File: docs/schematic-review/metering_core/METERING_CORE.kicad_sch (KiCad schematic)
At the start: 56 parts, among them U2 ATM90E26-YU, U4 ISO6721BD, U5 MAX3487E

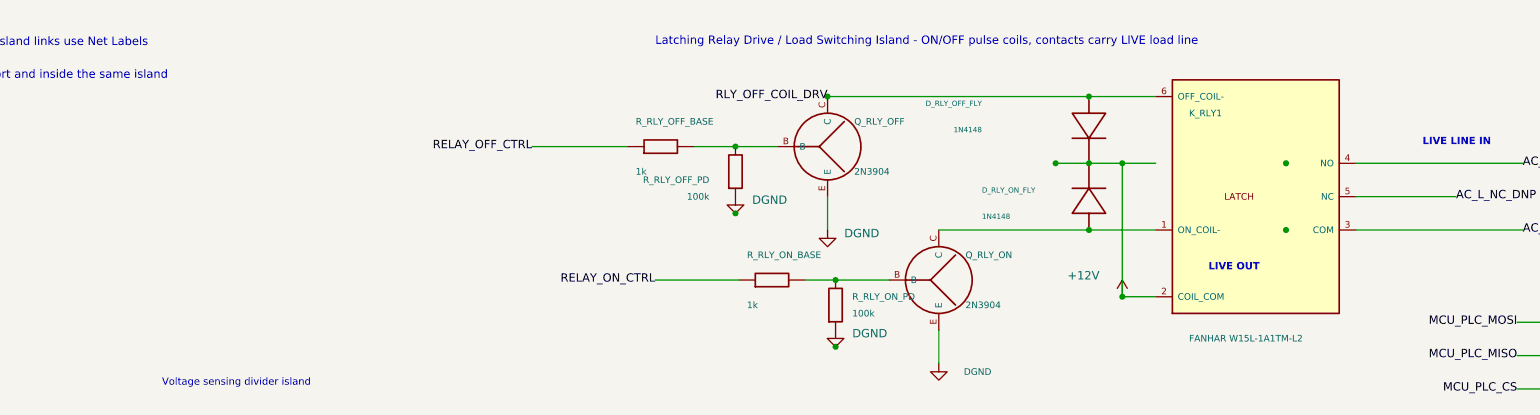
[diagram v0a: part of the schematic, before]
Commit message: Fix latching relay coil common routing
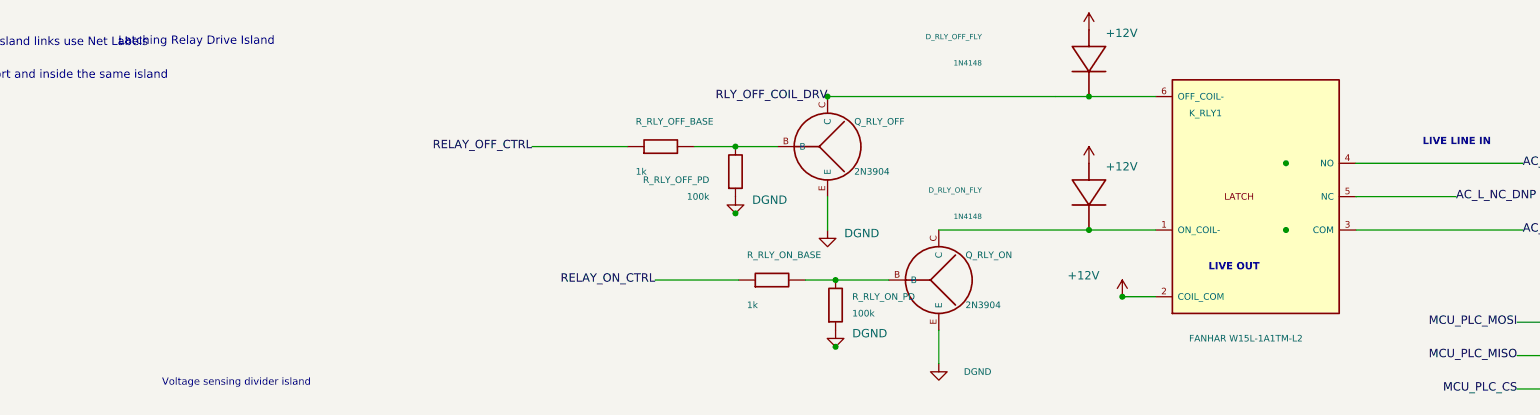
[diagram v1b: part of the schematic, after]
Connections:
- net +12V: now also D_RLY_OFF_FLY.A, D_RLY_ON_FLY.A; no longer D_RLY_OFF_FLY.K, D_RLY_ON_FLY.K
- net RLY_OFF_COIL_DRV: now also D_RLY_OFF_FLY.K; no longer D_RLY_OFF_FLY.A
- net at K_RLY1.1 (ON_COIL-), Q_RLY_ON.C: now also D_RLY_ON_FLY.K; no longer D_RLY_ON_FLY.A
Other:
- note added: "Latching Relay Drive Island"
- note removed: "Latching Relay Drive / Load Switching Island - ON/OFF pulse coils, contacts carry LIVE load line"
- moved on the sheet: D_RLY_OFF_FLY, D_RLY_ON_FLY
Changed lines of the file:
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@@
 		)
 	)
-	(text "Latching Relay Drive / Load Switching Island - ON/OFF pulse coils, contacts carry LIVE load line"
+	(text "Latching Relay Drive Island"
 		(exclude_from_sim no)
-		(at 208.76 20.32 0)
+		(at 127.00 20.32 0)
 		(effects
 			(font
@@
 	(wire
 		(pts
-			(xy 269.72 38.1) (xy 284.96 38.1)
-		)
-		(stroke
-			(width 0)
-			(type solid)
-		)
-	)
-	(wire
-		(pts
-			(xy 279.88 38.1) (xy 279.88 58.42)
-		)
-		(stroke
-			(width 0)
-			(type solid)
-		)
-	)
-	(wire
-		(pts
 			(xy 284.96 58.42) (xy 279.88 58.42)
 		)
@@
 		(instances (project "METERING_CORE" (path "/e4236fbb-ccab-4d10-bcea-7fda722d6751" (reference "#PWR_RLY_COIL_COM_12V") (unit 1))))
 	)
+	(symbol
+		(lib_id "power:+12V")
+		(at 274.80 17.78 0)
+		(unit 1)
+		(body_style 1)
+		(exclude_from_sim no)
+		(in_bom yes)
+		(on_board yes)
+		(in_pos_files yes)
+		(dnp no)
+		(property "Reference" "#PWR_RLY_OFF_FLY_12V"
+			(at 277.34 13.97 0)
+			(hide yes)
+			(show_name no)
+			(do_not_autoplace no)
+			(effects (font (size 1.27 1.27)))
+		)
+		(property "Value" "+12V"
+			(at 277.34 18.288 0)
+			(show_name no)
+			(do_not_autoplace no)
+			(effects (font (size 1.27 1.27)) (justify left))
+		)
+		(property "Footprint" "" (at 274.80 17.78 0) (show_name no) (do_not_autoplace no) (effects (font (size 1.27 1.27))))
+		(property "Datasheet" "" (at 274.80 17.78 0) (show_name no) (do_not_autoplace no) (effects (font (size 1.27 1.27))))
+		(property "Description" "" (at 274.80 17.78 0) (show_name no) (do_not_autoplace no) (effects (font (size 1.27 1.27))))
+		(pin "1")
+		(instances (project "METERING_CORE" (path "/e4236fbb-ccab-4d10-bcea-7fda722d6751" (reference "#PWR_RLY_OFF_FLY_12V") (unit 1))))
+	)
+	(symbol
+		(lib_id "power:+12V")
+		(at 274.80 38.10 0)
+		(unit 1)
+		(body_style 1)
+		(exclude_from_sim no)
+		(in_bom yes)
+		(on_board yes)
+		(in_pos_files yes)
+		(dnp no)
+		(property "Reference" "#PWR_RLY_ON_FLY_12V"
+			(at 277.34 34.29 0)
+			(hide yes)
+			(show_name no)
+			(do_not_autoplace no)
+			(effects (font (size 1.27 1.27)))
+		)
+		(property "Value" "+12V"
+			(at 277.34 38.608 0)
+			(show_name no)
+			(do_not_autoplace no)
+			(effects (font (size 1.27 1.27)) (justify left))
+		)
+		(property "Footprint" "" (at 274.80 38.10 0) (show_name no) (do_not_autoplace no) (effects (font (size 1.27 1.27))))
+		(property "Datasheet" "" (at 274.80 38.10 0) (show_name no) (do_not_autoplace no) (effects (font (size 1.27 1.27))))
+		(property "Description" "" (at 274.80 38.10 0) (show_name no) (do_not_autoplace no) (effects (font (size 1.27 1.27))))
+		(pin "1")
+		(instances (project "METERING_CORE" (path "/e4236fbb-ccab-4d10-bcea-7fda722d6751" (reference "#PWR_RLY_ON_FLY_12V") (unit 1))))
+	)
 	(wire
 		(pts
@@
 	(symbol
 		(lib_id "SmartLoad:D_Flyback_Island")
-		(at 274.8 43.18 0)
+		(at 274.8 43.18 180)
 		(unit 1)
 		(body_style 1)
@@
 	)
 	(junction
-		(at 269.72 38.1)
-		(diameter 0)
-		(color 0 0 0 0)
-	)
-	(junction
-		(at 279.88 38.1)
-		(diameter 0)
-		(color 0 0 0 0)
-	)
-	(junction
 		(at 279.88 58.42)
 		(diameter 0)
@@
 	(symbol
 		(lib_id "SmartLoad:D_Flyback_Island")
-		(at 274.80 33.02 180)
+		(at 274.80 22.86 180)
 		(unit 1)
 		(body_style 1)
@@
 		(in_pos_files yes)
 		(dnp no)
-		(property "Reference" "D_RLY_OFF_FLY" (at 258.50 29.00 0) (show_name no) (do_not_autoplace no) (effects (font (size 0.8 0.8)) (justify left)))
-		(property "Value" "1N4148" (at 258.50 33.00 0) (show_name no) (do_not_autoplace no) (effects (font (size 0.8 0.8)) (justify left)))
-		(property "Footprint" "SmartLoad:D_DO35_AK_Review" (at 304.80 33.02 0) (hide yes) (show_name no) (do_not_autoplace no) (effects (font (size 1 1))))
-		(property "Datasheet" "" (at 304.80 33.02 0) (hide yes) (show_name no) (do_not_autoplace no) (effects (font (size 1 1))))
-		(property "Description" "Flyback diode for OFF coil, same orientation as ON coil diode" (at 304.80 33.02 0) (hide yes) (show_name no) (do_not_autoplace no) (effects (font (size 1 1))))
+		(property "Reference" "D_RLY_OFF_FLY" (at 258.50 18.84 0) (show_name no) (do_not_autoplace no) (effects (font (size 0.8 0.8)) (justify left)))
+		(property "Value" "1N4148" (at 258.50 22.84 0) (show_name no) (do_not_autoplace no) (effects (font (size 0.8 0.8)) (justify left)))
+		(property "Footprint" "SmartLoad:D_DO35_AK_Review" (at 304.80 22.86 0) (hide yes) (show_name no) (do_not_autoplace no) (effects (font (size 1 1))))
+		(property "Datasheet" "" (at 304.80 22.86 0) (hide yes) (show_name no) (do_not_autoplace no) (effects (font (size 1 1))))
+		(property "Description" "Flyback diode for OFF coil, cathode to +12V power port and anode to OFF coil driver" (at 304.80 22.86 0) (hide yes) (show_name no) (do_not_autoplace no) (effects (font (size 1 1))))
 		(pin "K")
 		(pin "A")
@@
 		(diameter 0)
 		(color 0 0 0 0)
-	)
-	(junction
-		(at 274.80 38.10)
-		(diameter 0)
-		(color 0 0 0 0)

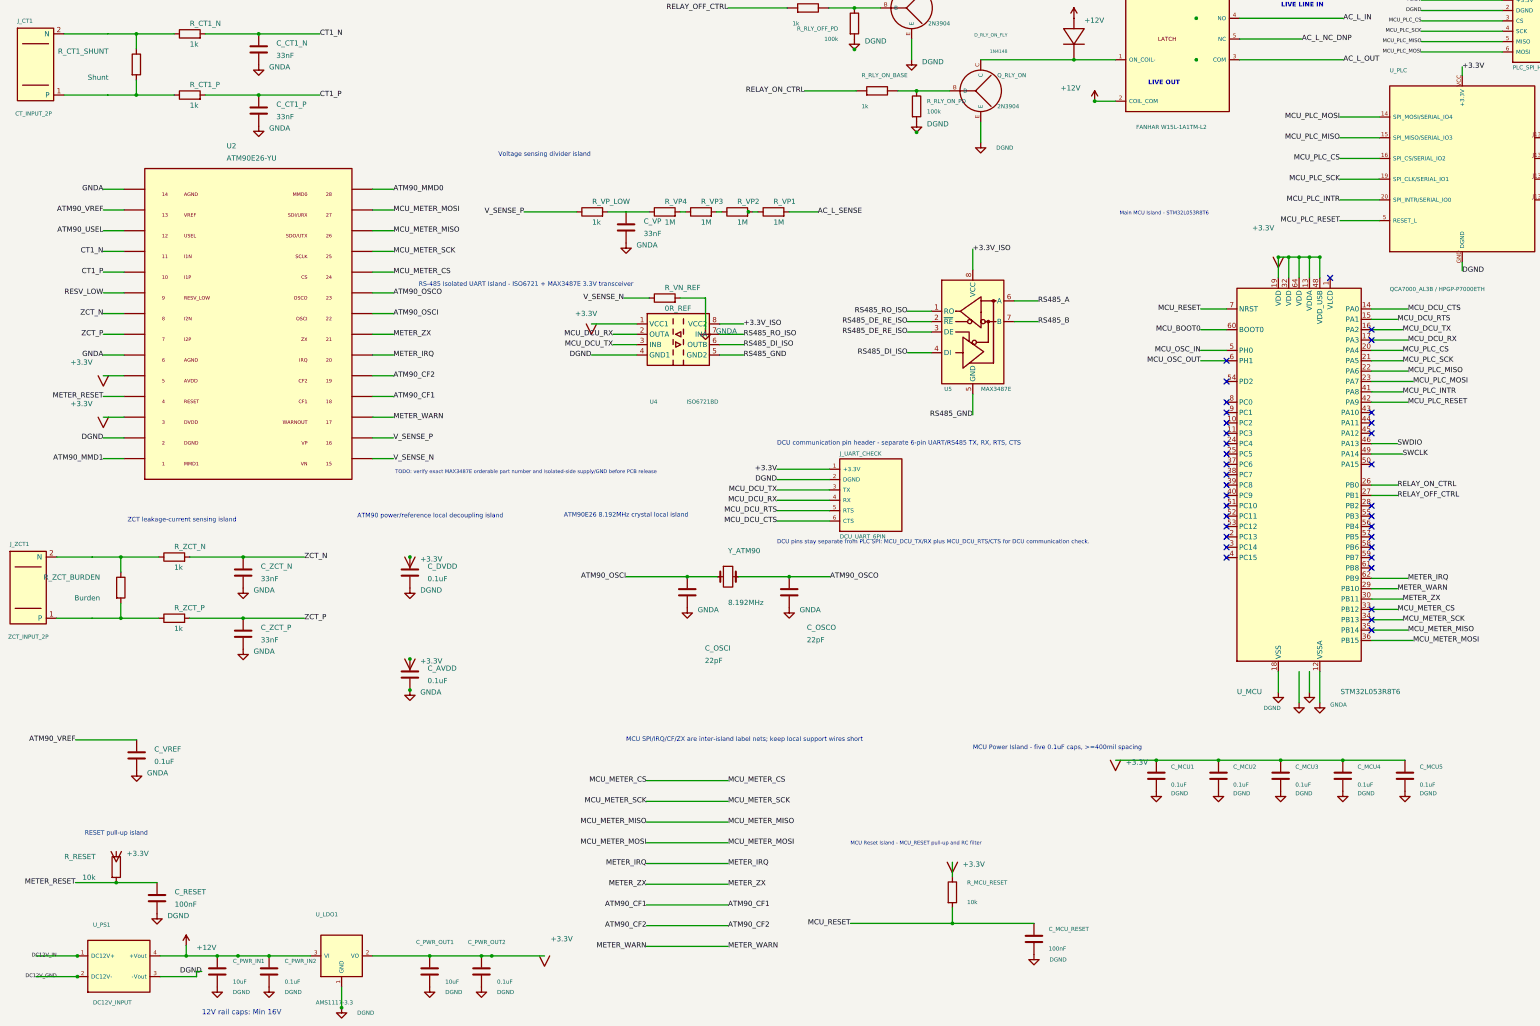
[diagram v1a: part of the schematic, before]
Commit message: Fix floating schematic ports and text clearance
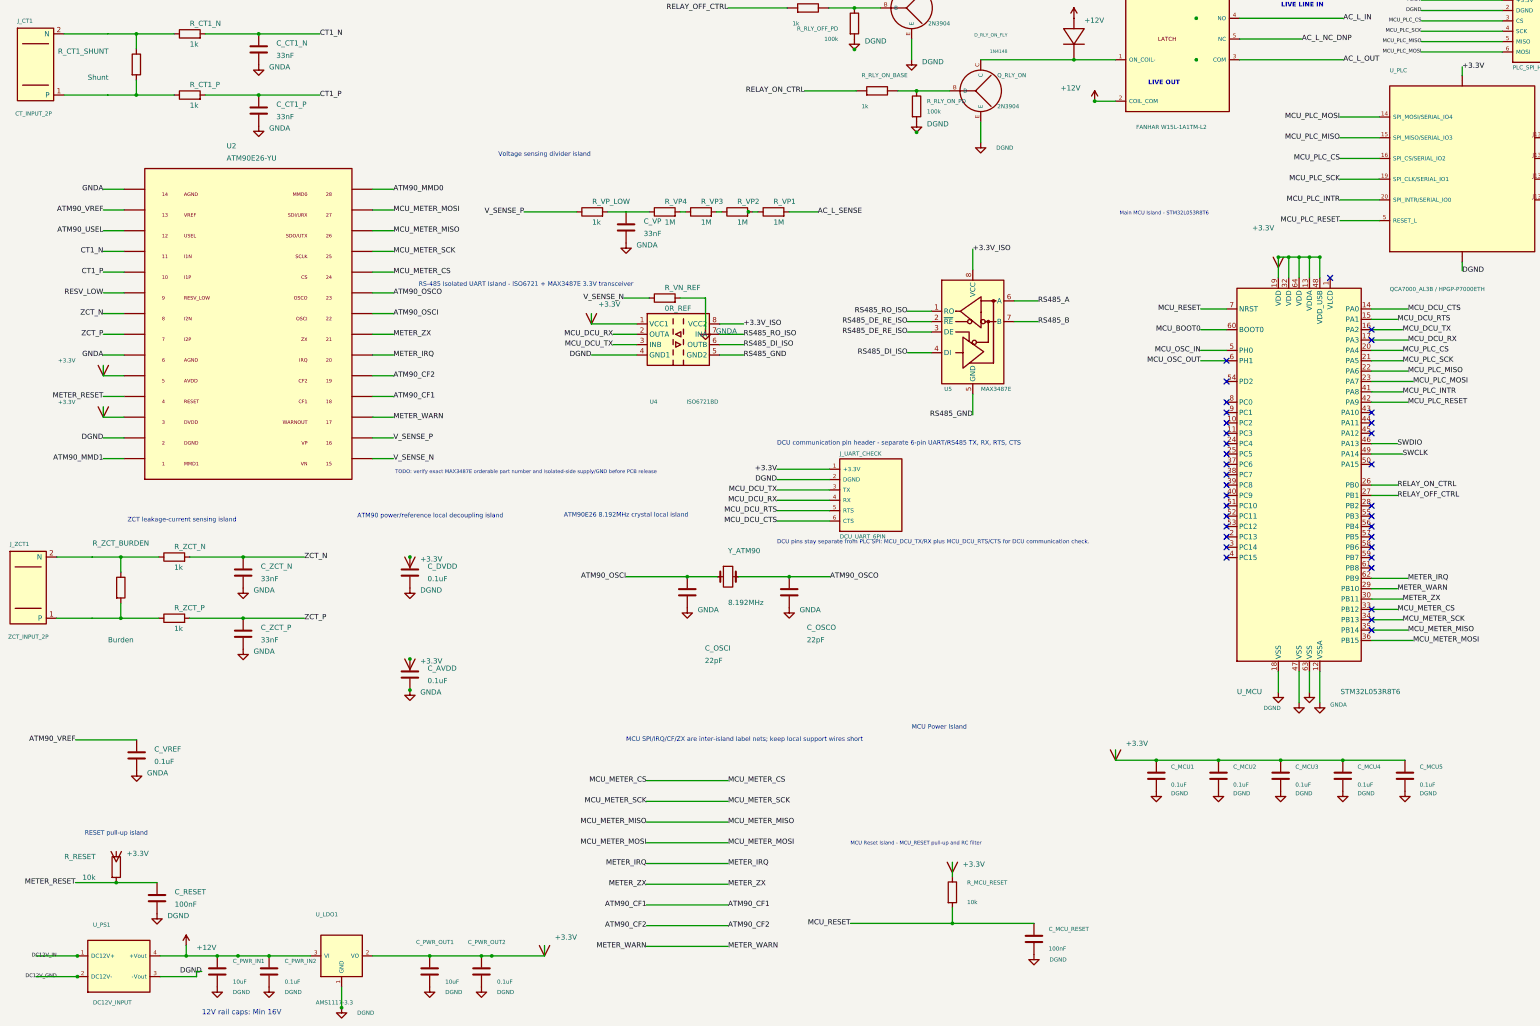
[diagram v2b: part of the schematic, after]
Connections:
- net DGND: now also U_MCU.63 (VSS)
- net GNDA: no longer U_MCU.63 (VSS)
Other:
- note added: "MCU Power Island"
- note removed: "MCU Power Island - five 0.1uF caps, >=400mil spacing"
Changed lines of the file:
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@@
 		(company "IOTECH")
 	)
-	(text "MCU Power Island - five 0.1uF caps, >=400mil spacing"
+	(text "MCU Power Island"
 		(exclude_from_sim no)
-		(at 250 217 0)
+		(at 235 212 0)
 		(effects
 			(font
@@
 	(wire
 		(pts
+			(xy 285 220) (xy 285 217.46)
+		)
+		(stroke
+			(width 0)
+			(type solid)
+		)
+	)
+	(wire
+		(pts
 			(xy 41.91 130.81) (xy 36.83 130.81)
 		)
@@
 	(wire
 		(pts
+			(xy 324.92 198.26) (xy 324.92 203.34)
+		)
+		(stroke
+			(width 0)
+			(type solid)
+		)
+	)
+	(wire
+		(pts
 			(xy 330 198.26) (xy 330 205.88)
 		)
@@
 	(wire
 		(pts
-			(xy 324.92 198.26) (xy 324.92 203.34)
+			(xy 332.54 198.26) (xy 332.54 203.34)
 		)
 		(stroke
@@
 	(wire
 		(pts
+			(xy 156.5 113.03) (xy 156.5 110.49)
+		)
+		(stroke
+			(width 0)
+			(type solid)
+		)
+	)
+	(wire
+		(pts
 			(xy 170 260.56) (xy 190 260.56)
 		)
@@
 	(wire
 		(pts
-			(xy 332.54 198.26) (xy 332.54 203.34)
-		)
-		(stroke
-			(width 0)
-			(type solid)
-		)
-	)
-	(wire
-		(pts
 			(xy 335.08 198.26) (xy 335.08 205.88)
 		)
@@
 	)
 	(symbol
-		(lib_id "power:GNDA")
+		(lib_id "power:DGND")
 		(at 332.54 203.34 0)
 		(unit 1)
@@
 		(in_pos_files yes)
 		(dnp no)
-		(property "Reference" "#PWR_MCU_BOTTOM_GNDA1" (at 335.08 199.53 0) (hide yes) (show_name no) (do_not_autoplace no) (effects (font (size 1.27 1.27))))
-		(property "Value" "GNDA" (at 335.1 202.3 0) (hide yes) (show_name no) (do_not_autoplace no) (effects (font (size 1.0 1.0)) (justify left)))
+		(property "Reference" "#PWR_MCU_BOTTOM_DGND3" (at 335.08 199.53 0) (hide yes) (show_name no) (do_not_autoplace no) (effects (font (size 1.27 1.27))))
+		(property "Value" "DGND" (at 335.1 202.3 0) (hide yes) (show_name no) (do_not_autoplace no) (effects (font (size 1.0 1.0)) (justify left)))
 		(property "Footprint" "" (at 332.54 203.34 0) (show_name no) (do_not_autoplace no) (effects (font (size 1.27 1.27))))
 		(property "Datasheet" "" (at 332.54 203.34 0) (show_name no) (do_not_autoplace no) (effects (font (size 1.27 1.27))))
 		(property "Description" "" (at 332.54 203.34 0) (show_name no) (do_not_autoplace no) (effects (font (size 1.27 1.27))))
 		(pin "1")
-		(instances (project "METERING_CORE" (path "/e4236fbb-ccab-4d10-bcea-7fda722d6751" (reference "#PWR_MCU_BOTTOM_GNDA1") (unit 1))))
+		(instances (project "METERING_CORE" (path "/e4236fbb-ccab-4d10-bcea-7fda722d6751" (reference "#PWR_MCU_BOTTOM_DGND3") (unit 1))))
 	)
 	(symbol
@@
 	(wire
 		(pts
+			(xy 36.83 125.73) (xy 36.83 123.19)
+		)
+		(stroke
+			(width 0)
+			(type solid)
+		)
+	)
+	(wire
+		(pts
 			(xy 187.96 115.57) (xy 193.8 115.57)
 		)
@@
 	(wire
 		(pts
+			(xy 36.83 135.89) (xy 36.83 133.35)
+		)
+		(stroke
+			(width 0)
+			(type solid)
+		)
+	)
+	(wire
+		(pts
 			(xy 41.91 105.41) (xy 36.83 105.41)
 		)
@@
 	(wire
 		(pts
+			(xy 145 267.97) (xy 145 265.43)
+		)
+		(stroke
+			(width 0)
+			(type solid)
+		)
+	)
+	(wire
+		(pts
 			(xy 34.12 170.18) (xy 50.41 170.18)
 		)
@@
 	(symbol
 		(lib_id "power:+3.3V")
-		(at 156.5 113.03 0)
+		(at 156.5 110.49 0)
 		(unit 1)
 		(body_style 1)
@@
 		(dnp no)
 		(property "Reference" "#PWR_AUTO_33V_006"
-			(at 159.04 109.22 0)
+			(at 159.04 106.68 0)
 			(hide yes)
 			(show_name no)
@@
 		)
 		(property "Value" "+3.3V"
-			(at 152.5 110.5 0)
+			(at 158.2 108.2 0)
 			(show_name no)
 			(do_not_autoplace no)
@@
 		)
 		(property "Footprint" ""
-			(at 156.5 113.03 0)
+			(at 156.5 110.49 0)
 			(show_name no)
 			(do_not_autoplace no)
@@
 		)
 		(property "Datasheet" ""
-			(at 156.5 113.03 0)
+			(at 156.5 110.49 0)
 			(show_name no)
 			(do_not_autoplace no)
@@
 		)
 		(property "Description" ""
-			(at 156.5 113.03 0)
+			(at 156.5 110.49 0)
 			(show_name no)
 			(do_not_autoplace no)
@@
 	(symbol
 		(lib_id "power:+3.3V")
-		(at 36.83 135.89 0)
+		(at 36.83 133.35 0)
 		(unit 1)
 		(body_style 1)
@@
 		(dnp no)
 		(property "Reference" "#PWR_AUTO_33V_007"
-			(at 39.37 132.08 0)
+			(at 39.37 129.54 0)
 			(hide yes)
 			(show_name no)
@@
 		)
 		(property "Value" "+3.3V"
-			(at 34.2 132.6 0)
+			(at 30.0 132.2 0)
 			(show_name no)
 			(do_not_autoplace no)
-			(effects (font (size 1.27 1.27)) (justify right))
+			(effects (font (size 1.0 1.0)) (justify right))
 		)
 		(property "Footprint" ""
-			(at 36.83 135.89 0)
+			(at 36.83 133.35 0)
 			(show_name no)
 			(do_not_autoplace no)
@@
 		)
 		(property "Datasheet" ""
-			(at 36.83 135.89 0)
+			(at 36.83 133.35 0)
 			(show_name no)
 			(do_not_autoplace no)
@@
 		)
 		(property "Description" ""
-			(at 36.83 135.89 0)
+			(at 36.83 133.35 0)
 			(show_name no)
 			(do_not_autoplace no)
@@
 	(symbol
 		(lib_id "power:+3.3V")
-		(at 36.83 125.73 0)
+		(at 36.83 123.19 0)
 		(unit 1)
 		(body_style 1)
@@
 		(dnp no)
 		(property "Reference" "#PWR_AUTO_33V_008"
-			(at 39.37 121.92 0)
+			(at 39.37 119.38 0)
 			(hide yes)
 			(show_name no)
@@
 		)
 		(property "Value" "+3.3V"
-			(at 34.2 122.44 0)
+			(at 30.0 122.0 0)
 			(show_name no)
 			(do_not_autoplace no)
-			(effects (font (size 1.27 1.27)) (justify right))
+			(effects (font (size 1.0 1.0)) (justify right))
 		)
 		(property "Footprint" ""
-			(at 36.83 125.73 0)
+			(at 36.83 123.19 0)
 			(show_name no)
 			(do_not_autoplace no)
@@
 		)
 		(property "Datasheet" ""
-			(at 36.83 125.73 0)
+			(at 36.83 123.19 0)
 			(show_name no)
 			(do_not_autoplace no)
@@
 		)
 		(property "Description" ""
-			(at 36.83 125.73 0)
+			(at 36.83 123.19 0)
 			(show_name no)
 			(do_not_autoplace no)
@@
 	(symbol
 		(lib_id "power:+3.3V")
-		(at 145 267.97 0)
+		(at 145 265.43 0)
 		(unit 1)
 		(body_style 1)
@@
 		(dnp no)
 		(property "Reference" "#PWR_AUTO_33V_010"
-			(at 147.54 264.16 0)
+			(at 147.54 261.62 0)
 			(hide yes)
 			(show_name no)
@@
 		)
 		(property "Value" "+3.3V"
-			(at 146.5 263.8 0)
+			(at 147.54 263.4 0)
 			(show_name no)
 			(do_not_autoplace no)
@@
 		)
 		(property "Footprint" ""
-			(at 145 267.97 0)
+			(at 145 265.43 0)
 			(show_name no)
 			(do_not_autoplace no)
@@
 		)
 		(property "Datasheet" ""
-			(at 145 267.97 0)
+			(at 145 265.43 0)
 			(show_name no)
 			(do_not_autoplace no)
@@
 		)
 		(property "Description" ""
-			(at 145 267.97 0)
+			(at 145 265.43 0)
 			(show_name no)
 			(do_not_autoplace no)
@@
 		(dnp no)
 		(property "Reference" "R_ZCT_BURDEN"
-			(at 36.04 175.14 0)
+			(at 41.12 166.80 0)
 			(show_name no)
 			(do_not_autoplace no)
@@
 					(size 1.27 1.27)
 				)
-				(justify right)
 			)
 		)
 		(property "Value" "Burden"
-			(at 36.04 180.22 0)
+			(at 41.12 190.50 0)
 			(show_name no)
 			(do_not_autoplace no)
@@
 					(size 1.27 1.27)
 				)
-				(justify right)
 			)
 		)
@@
 	(symbol
 		(lib_id "power:+3.3V")
-		(at 285 220 0)
+		(at 285 217.46 0)
 		(unit 1)
 		(body_style 1)
@@
 		(dnp no)
 		(property "Reference" "#PWR_MCU33"
-			(at 287.54 216.19 0)
+			(at 287.54 213.65 0)
 			(hide yes)
 			(show_name no)
@@
 		)
 		(property "Value" "+3.3V"
-			(at 287.54 220.51 0)
+			(at 287.54 215.90 0)
 			(show_name no)
 			(do_not_autoplace no)
@@
 		)
 		(property "Footprint" ""
-			(at 285 220 0)
+			(at 285 217.46 0)
 			(show_name no)
 			(do_not_autoplace no)
@@
 		)
 		(property "Datasheet" ""
-			(at 285 220 0)
+			(at 285 217.46 0)
 			(show_name no)
 			(do_not_autoplace no)
@@
 		)
 		(property "Description" ""
-			(at 285 220 0)
+			(at 285 217.46 0)
 			(show_name no)
 			(do_not_autoplace no)
